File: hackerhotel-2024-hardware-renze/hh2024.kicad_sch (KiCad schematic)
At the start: 48 parts, among them J1 SAO, J3 Micro_SD_Card, J4 USB-C, K1 SANYOU_SRD_Form_C, Q3 AP2302B, SW1 Multi-Directional-Switches, SW2 Multi-Directional-Switches, SW3 Multi-Directional-Switches, SW4 Multi-Directional-Switches, SW5 Multi-Directional-Switches, U5 CH32V003F4U6

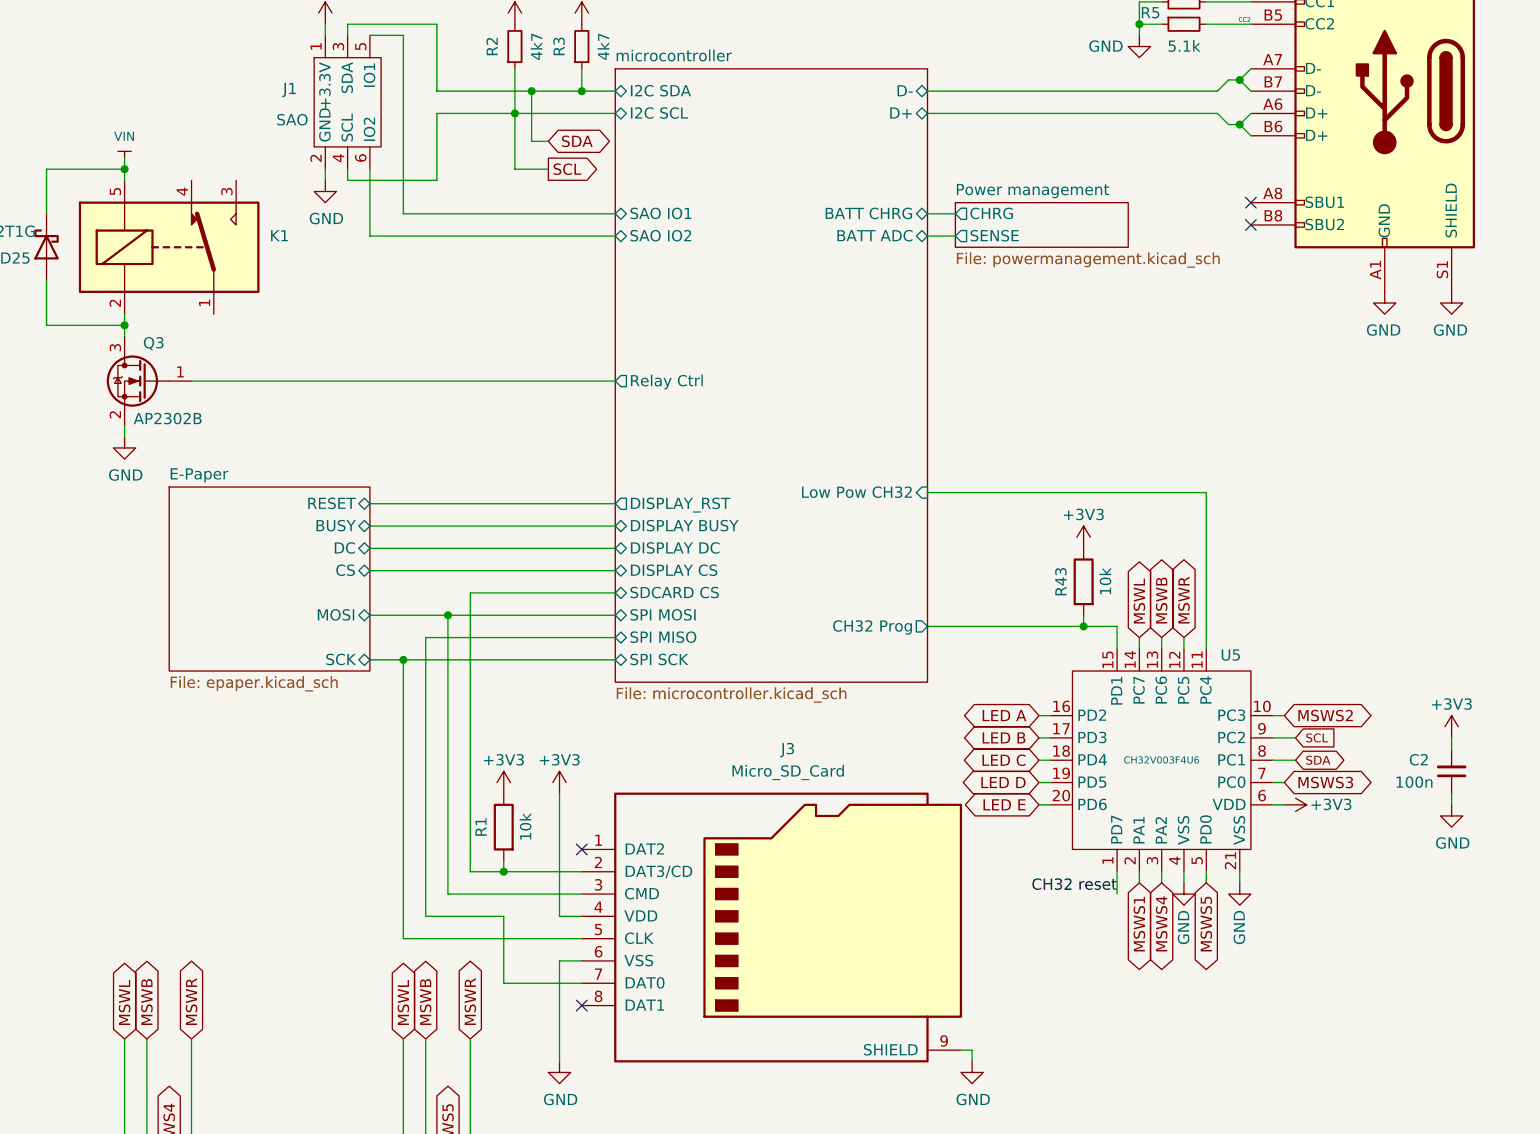
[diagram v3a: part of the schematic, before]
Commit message: Routing complete (apart from LEDs)
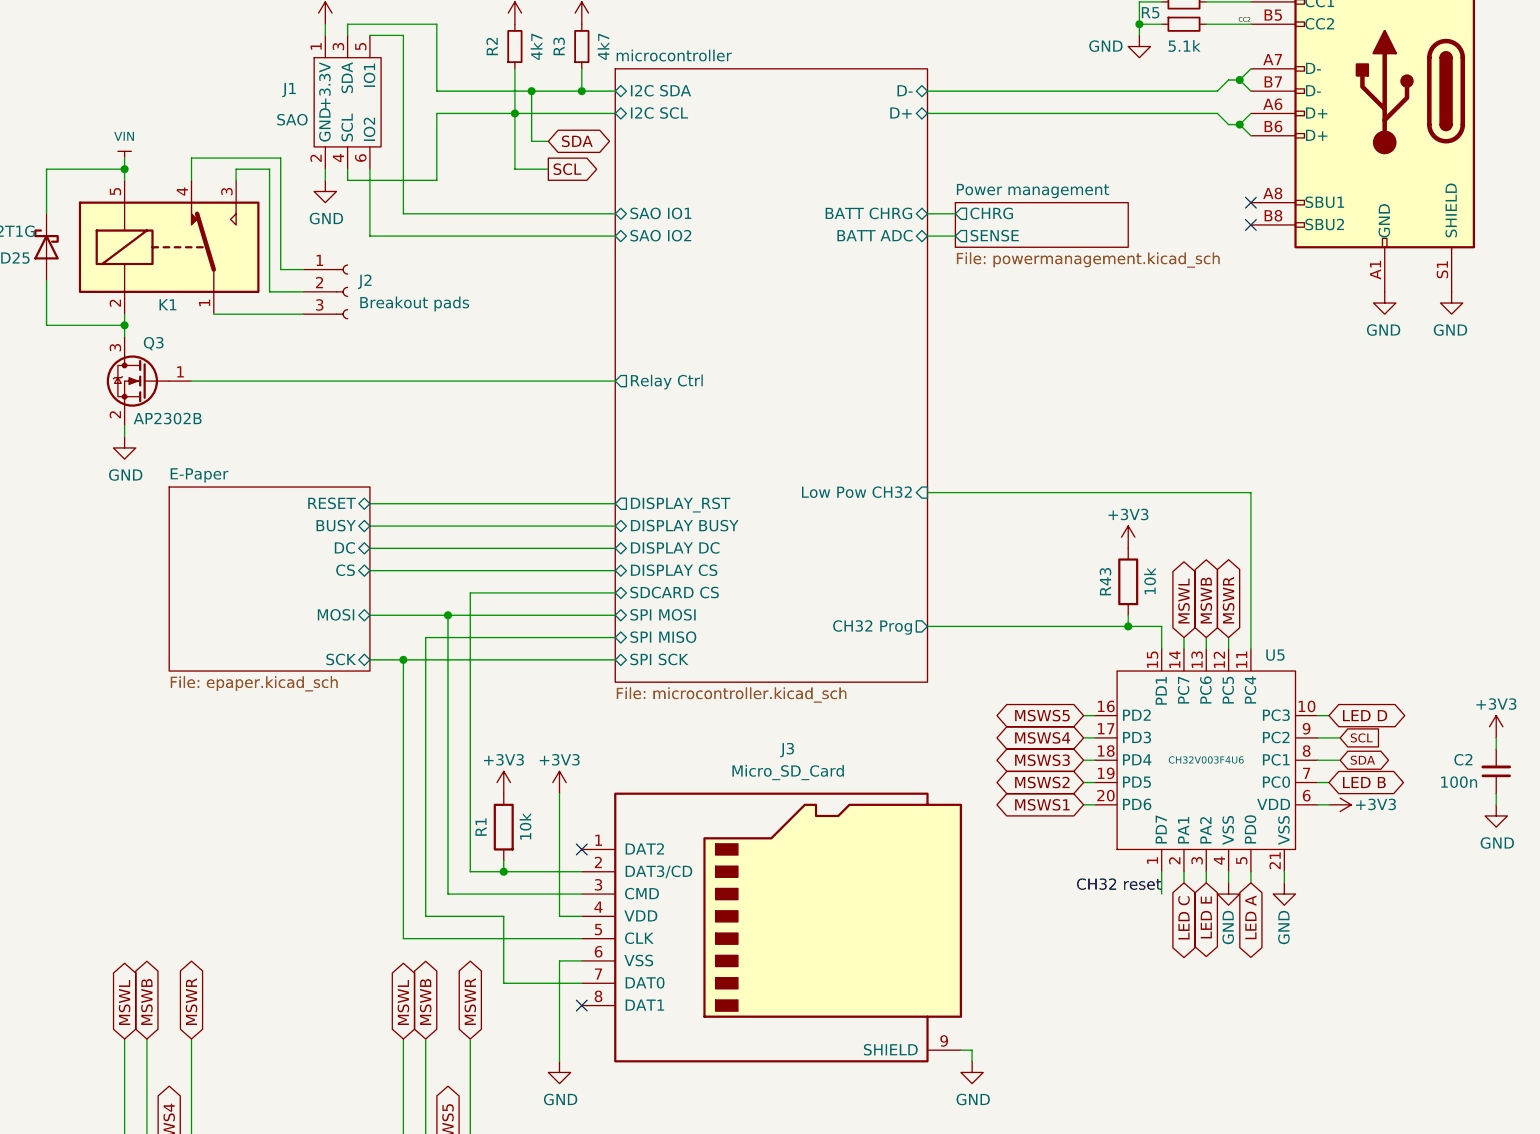
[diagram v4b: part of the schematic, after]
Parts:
- added J2: Breakout pads, Connector_PinHeader_2.54mm:PinHeader_1x03_P2.54mm_Vertical, symbol Connector:Conn_01x03_Socket
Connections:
- net LED A: now also U5.5 (PD0); no longer U5.16 (PD2)
- net LED B: now also U5.7 (PC0); no longer U5.17 (PD3)
- net LED C: now also U5.2 (PA1); no longer U5.18 (PD4)
- net LED D: now also U5.10 (PC3); no longer U5.19 (PD5)
- net LED E: now also U5.3 (PA2); no longer U5.20 (PD6)
- net MSWS1: now also U5.20 (PD6); no longer U5.2 (PA1)
- net MSWS2: now also U5.19 (PD5); no longer U5.10 (PC3)
- net MSWS3: now also U5.18 (PD4); no longer U5.7 (PC0)
- net MSWS4: now also U5.17 (PD3); no longer U5.3 (PA2)
- net MSWS5: now also U5.16 (PD2); no longer U5.5 (PD0)
- net at K1.1: now also J2.3 (Pin_3)
- net at K1.3: now also J2.2 (Pin_2)
- net at K1.4: now also J2.1 (Pin_1)
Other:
- moved on the sheet: C2, R43, U5

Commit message: routing almost finished
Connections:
- net A: no longer D11.1 (K), D12.2 (A), D13.2 (A), D15.1 (K), D16.2 (A), D17.1 (K), D17.2 (A), D18.1 (K), D20.1 (K), D22.1 (K), D24.1 (K), D5.2 (A), D6.2 (A), D7.1 (K), D7.2 (A), D8.2 (A), R23.2, R25.2
- net B: no longer D10.2 (A), D11.2 (A), D15.2 (A), D16.1 (K), D19.1 (K), D23.1 (K), D8.1 (K), D9.2 (A), R24.2
- new net C: D11.1 (K), D12.2 (A), D13.2 (A), D16.2 (A), D17.2 (A), D18.1 (K), D22.1 (K), D7.1 (K), R25.2
- new net D: D10.2 (A), D11.2 (A), D15.2 (A), D16.1 (K), D19.1 (K), D23.1 (K), D8.1 (K), D9.2 (A), R24.2
- new net E: D15.1 (K), D17.1 (K), D20.1 (K), D24.1 (K), D5.2 (A), D6.2 (A), D7.2 (A), D8.2 (A), R23.2

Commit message: Routing and BOM completed, missing art and regulator update
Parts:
- C2: LCSC C282519 -> C476766; Link (none) -> https://www.lcsc.com/product-detail/Multilayer-Ceramic-Capa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
- D10, D11, D12, D13, D14, D15, D16, D17, D18, D19, D20, D21, D22, D23, D24, D5, D6, D7, D8, D9: LCSC (none) -> C965861; Link (none) -> https://www.lcsc.com/product-detail/Light-Emitting-Diodes-L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
- D25: value NSVR0320MW2T1G -> NSR0320MW2T1G; LCSC C232573 -> C48192; Link (none) -> https://www.lcsc.com/product-detail/Schottky-Barrier-Diodes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
- F1: Link (none) -> https://www.lcsc.com/product-detail/Resettable-Fuses_Bright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
- J1: LCSC (none) -> C2829893; Link (none) -> https://www.lcsc.com/product-detail/Female-Headers_Lianshen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
- J2: LCSC (none) -> C2935909; Link (none) -> https://www.lcsc.com/product-detail/span-style-background-c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; now not fitted
- J3: Link (none) -> https://www.lcsc.com/product-detail/SD-Card-Connectors_SOFN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
- J4: Link (none) -> https://www.lcsc.com/product-detail/USB-Connectors_Korean-H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
- K1: LCSC (none) -> C136110; Link (none) -> https://www.lcsc.com/product-detail/Signal-Relays_Zhejiang-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
- Q3: Link (none) -> https://www.lcsc.com/product-detail/MOSFETs_ALLPOWER-ShenZh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
- R1, R28, R29, R30, R43: LCSC C25744 -> C5140188; Link (none) -> https://www.lcsc.com/product-detail/Chip-span-style-backgro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
- R2, R3: value 4k7 -> 4.7k; LCSC C25900 -> C2907326; Link (none) -> https://www.lcsc.com/product-detail/Chip-span-style-backgro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
- R23, R24, R25, R26, R27: LCSC (none) -> C25305; Link (none) -> https://www.lcsc.com/product-detail/Chip-Resistor-Surface-M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
- R4, R5: LCSC C25905 -> C2930296; Link (none) -> https://www.lcsc.com/product-detail/Chip-span-style-backgro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
- SW1, SW2, SW3, SW4, SW5: LCSC (none) -> C318951; Link (none) -> https://www.lcsc.com/product-detail/Multi-Directional-Switc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
- U5: Link (none) -> https://www.lcsc.com/product-detail/Microcontroller-Units-M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

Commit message: V1 complete
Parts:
- added R33: 0, Resistor_SMD:R_0805_2012Metric, symbol symbols:R
- added R34: 10k, Resistor_SMD:R_0805_2012Metric, symbol symbols:R
- added R35: 1k, Resistor_SMD:R_0805_2012Metric, symbol symbols:R
- added TP1, TP2, TP6: TestPoint, TestPoint:TestPoint_Pad_1.0x1.0mm, symbol Connector:TestPoint
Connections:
- net +3V3: now also R34.1
- net CH32 reset: now also TP1.1
- net GND: now also TP6.1
- net microcontroller/CH32 Prog: now also R33.1; no longer R43.2, U5.15 (PD1)
- net microcontroller/Low Pow CH32: now also R34.2
- net microcontroller/Relay Ctrl: now also R35.2; no longer Q3.1 (G)
- new net: R33.2, R43.2, TP2.1, U5.15 (PD1)
- new net: Q3.1 (G), R35.1
